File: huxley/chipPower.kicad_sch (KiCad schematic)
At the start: 5 parts, among them J1 Conn_01x01_Socket, J2 Conn_01x01_Socket, J3 Conn_01x01_Socket, J4 Conn_Coaxial_Power

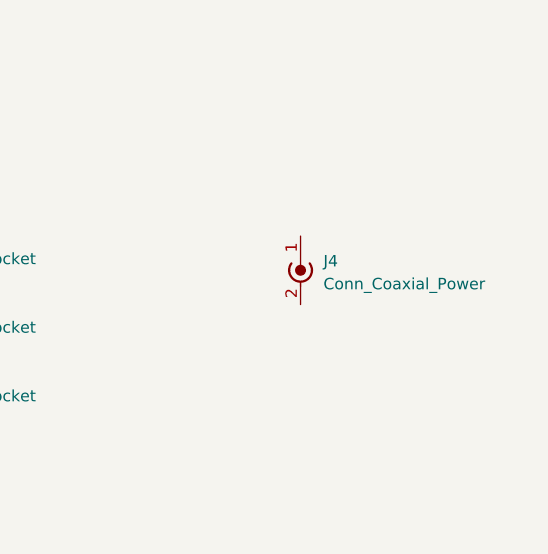
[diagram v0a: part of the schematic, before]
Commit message: added analog chip schematics and connector footprints
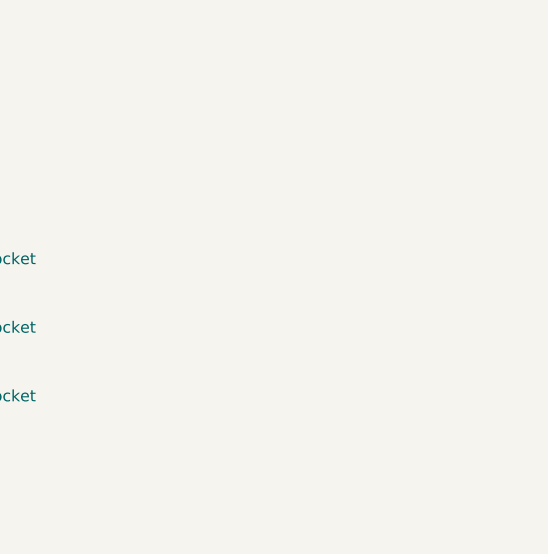
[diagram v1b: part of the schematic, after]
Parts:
- removed J4: Conn_Coaxial_Power, symbol Connector:Conn_Coaxial_Power
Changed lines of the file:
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@@
-	)
-	(symbol
-		(lib_id "Connector:Conn_Coaxial_Power")
-		(at 190.5 55.88 0)
-		(unit 1)
-		(exclude_from_sim no)
-		(in_bom yes)
-		(on_board yes)
-		(dnp no)
-		(fields_autoplaced yes)
-		(property "Reference" "J4"
-			(at 193.04 56.1339 0)
-			(effects
-				(font
-					(size 1.27 1.27)
-				)
-				(justify left)
-			)
-		)
-		(property "Value" "Conn_Coaxial_Power"
-			(at 193.04 58.6739 0)
-			(effects
-				(font
-					(size 1.27 1.27)
-				)
-				(justify left)
-			)
-		)
-		(property "Footprint" ""
-			(at 190.5 57.15 0)
-			(effects
-				(font
-					(size 1.27 1.27)
-				)
-				(hide yes)
-			)
-		)
-		(property "Datasheet" "~"
-			(at 190.5 57.15 0)
-			(effects
-				(font
-					(size 1.27 1.27)
-				)
-				(hide yes)
-			)
-		)
-		(property "Description" "coaxial connector (BNC, SMA, SMB, SMC, Cinch/RCA, LEMO, ...)"
-			(at 190.5 55.88 0)
-			(effects
-				(font
-					(size 1.27 1.27)
-				)
-				(hide yes)
-			)
-		)
-		(pin "1"
-		)
-		(pin "2"
-		)
-		(instances
-			(project "huxley"
-				(path "/c6103430-c27a-4e90-8e2e-9404255f5ee3/ab3d06fa-a7a0-4394-b6d7-1ca538756c6f"
-					(reference "J4")
-					(unit 1)
-				)
-			)
-		)
 	)
 	(symbol

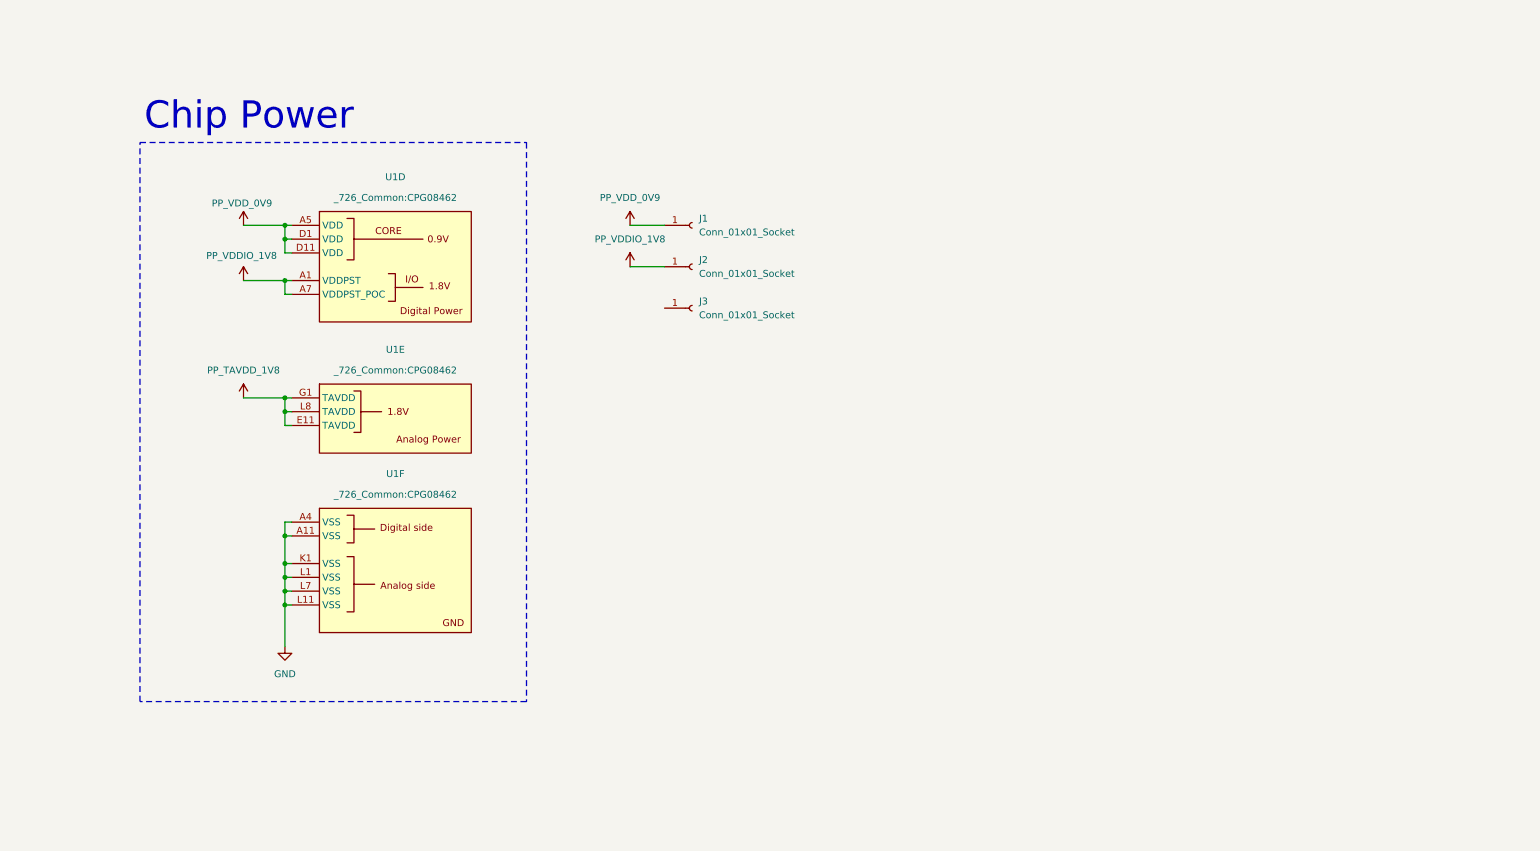
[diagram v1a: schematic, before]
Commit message: updated Ibias gen and footprints
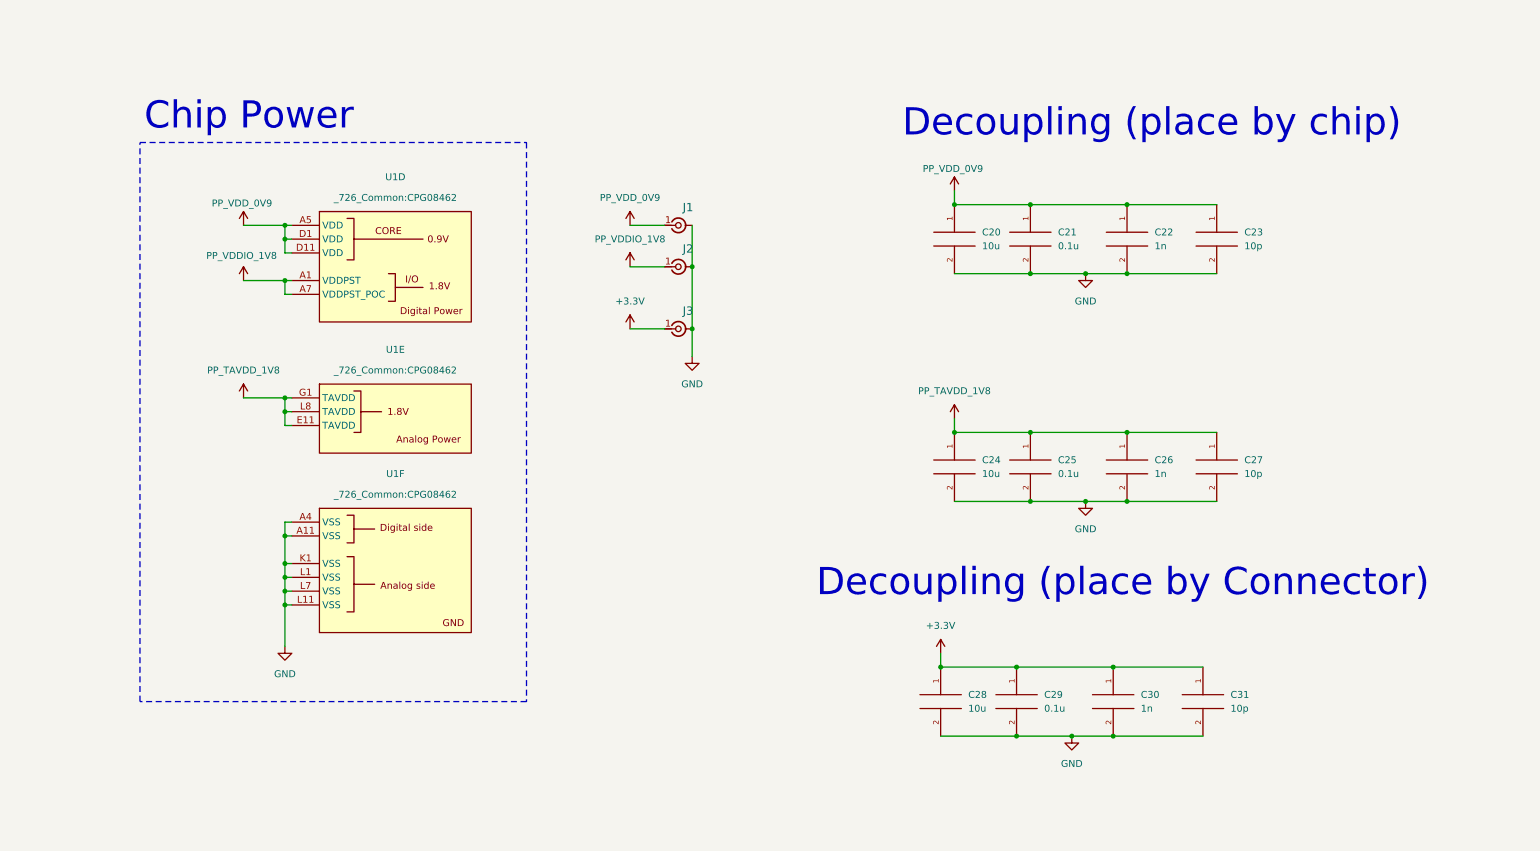
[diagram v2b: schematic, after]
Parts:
- removed J1, J2, J3: Conn_01x01_Socket, symbol Connector:Conn_01x01_Socket
- added C20, C24, C28: 10u, Capacitor_SMD:C_0402_1005Metric, symbol pspice:C
- added C21, C25, C29: 0.1u, Capacitor_SMD:C_0402_1005Metric, symbol pspice:C
- added C22, C26, C30: 1n, Capacitor_SMD:C_0402_1005Metric, symbol pspice:C
- added C23, C27, C31: 10p, Capacitor_SMD:C_0402_1005Metric, symbol pspice:C
- added J1, J2, J3: SMA_RF2-04A-T-00-50-G, 726_footprints:CONN_RF2-04A-T-00-50-G_ADM, symbol _PHASE:SMA_RF2-04A-T-00-50-G
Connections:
- net GND: now also C20.2, C21.2, C22.2, C23.2, C24.2, C25.2, C26.2, C27.2, C28.2, C29.2, C30.2, C31.2, J1., J1.3 (Ext), J1.4 (Ext), J1.5 (Ext), J2., J2.3 (Ext), J2.4 (Ext), J2.5 (Ext), J3., J3.3 (Ext), J3.4 (Ext), J3.5 (Ext)
- net PP_TAVDD_1V8: now also C24.1, C25.1, C26.1, C27.1
- net PP_VDDIO_1V8: now also J2.1
- net PP_VDD_0V9: now also C20.1, C21.1, C22.1, C23.1, J1.1
- new net +3.3V: C28.1, C29.1, C30.1, C31.1, J3.1
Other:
- note added: "Decoupling (place by Connector)"
- note added: "Decoupling (place by chip)"

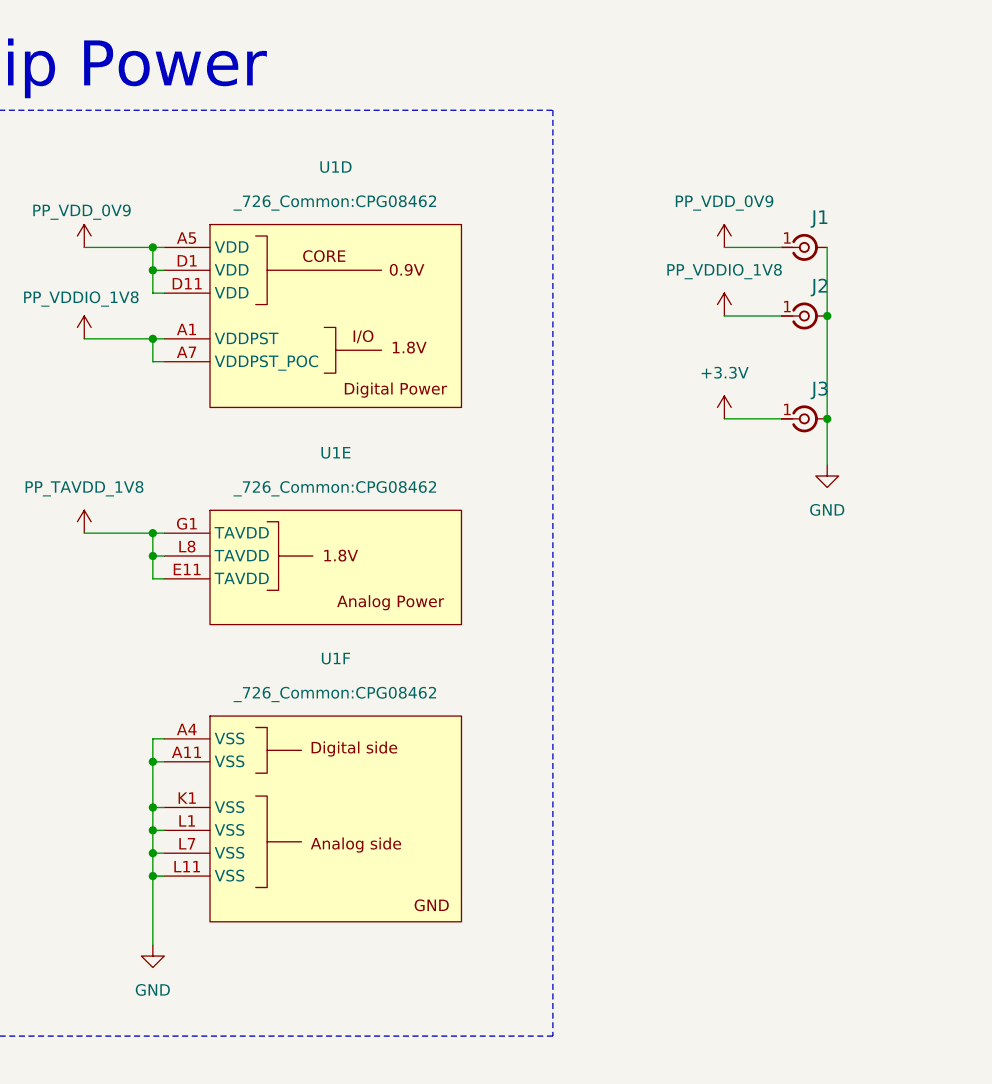
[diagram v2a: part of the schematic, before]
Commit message: updated footprints
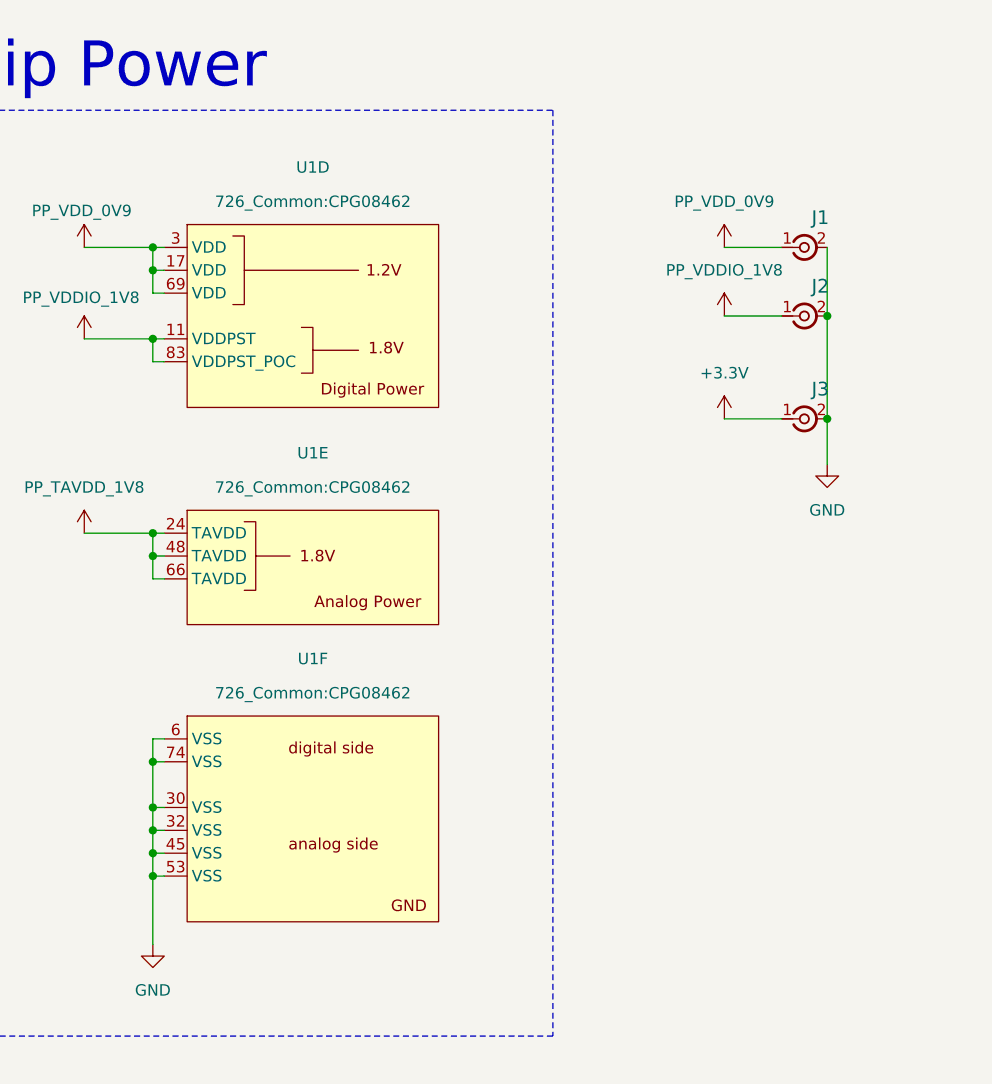
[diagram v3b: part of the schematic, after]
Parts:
- U1: footprint _726_Common:CPG08462 -> 726_Common:CPG08462
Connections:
- net GND: now also J1.2, J2.2, J3.2, U1.30 (VSS), U1.32 (VSS), U1.45 (VSS), U1.53 (VSS), U1.6 (VSS), U1.74 (VSS); no longer J1., J2., J3., U1.A11 (VSS), U1.A4 (VSS), U1.K1 (VSS), U1.L1 (VSS), U1.L11 (VSS), U1.L7 (VSS)
- net PP_TAVDD_1V8: now also U1.24 (TAVDD), U1.48 (TAVDD), U1.66 (TAVDD); no longer U1.E11 (TAVDD), U1.G1 (TAVDD), U1.L8 (TAVDD)
- net PP_VDDIO_1V8: now also U1.11 (VDDPST), U1.83 (VDDPST_POC); no longer U1.A1 (VDDPST), U1.A7 (VDDPST_POC)
- net PP_VDD_0V9: now also U1.17 (VDD), U1.3 (VDD), U1.69 (VDD); no longer U1.A5 (VDD), U1.D1 (VDD), U1.D11 (VDD)
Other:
- moved on the sheet: U1E

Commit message: layout
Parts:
- added C32: 10u, Capacitor_SMD:C_0402_1005Metric, symbol pspice:C
- added C33: 0.1u, Capacitor_SMD:C_0402_1005Metric, symbol pspice:C
- added C34: 1n, Capacitor_SMD:C_0402_1005Metric, symbol pspice:C
- added C35: 10p, Capacitor_SMD:C_0402_1005Metric, symbol pspice:C
- added J5: SMA_RF2-04A-T-00-50-G, 726_footprints:CONN_RF2-04A-T-00-50-G_ADM, symbol _PHASE:SMA_RF2-04A-T-00-50-G
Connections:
- net GND: now also C32.2, C33.2, C34.2, C35.2, J5.2, J5.3 (Ext), J5.4 (Ext), J5.5 (Ext)
- net PP_TAVDD_1V8: now also J5.1
- net PP_VDDIO_1V8: now also C32.1, C33.1, C34.1, C35.1
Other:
- moved on the sheet: C20, C21, C22, C23

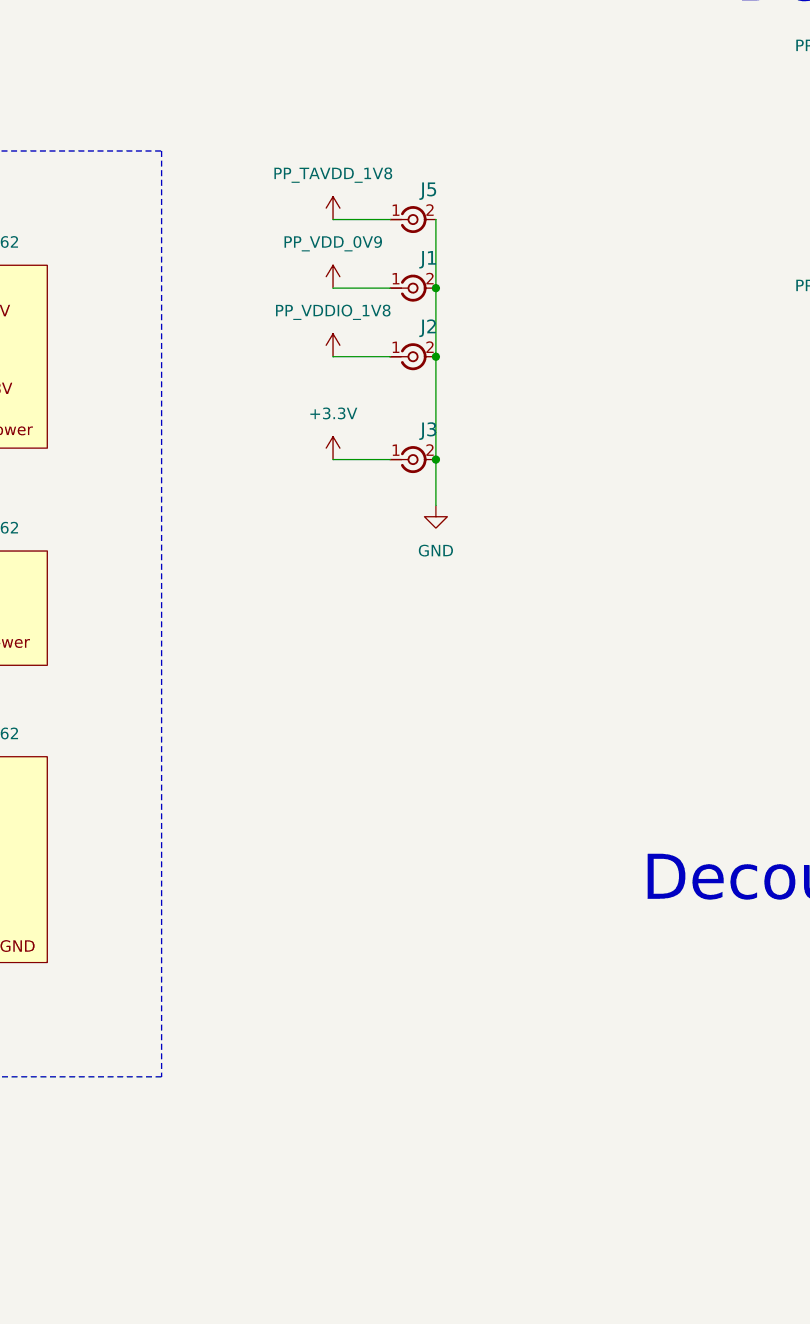
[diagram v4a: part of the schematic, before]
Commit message: added banana plugs and fixed analog discovery pinout
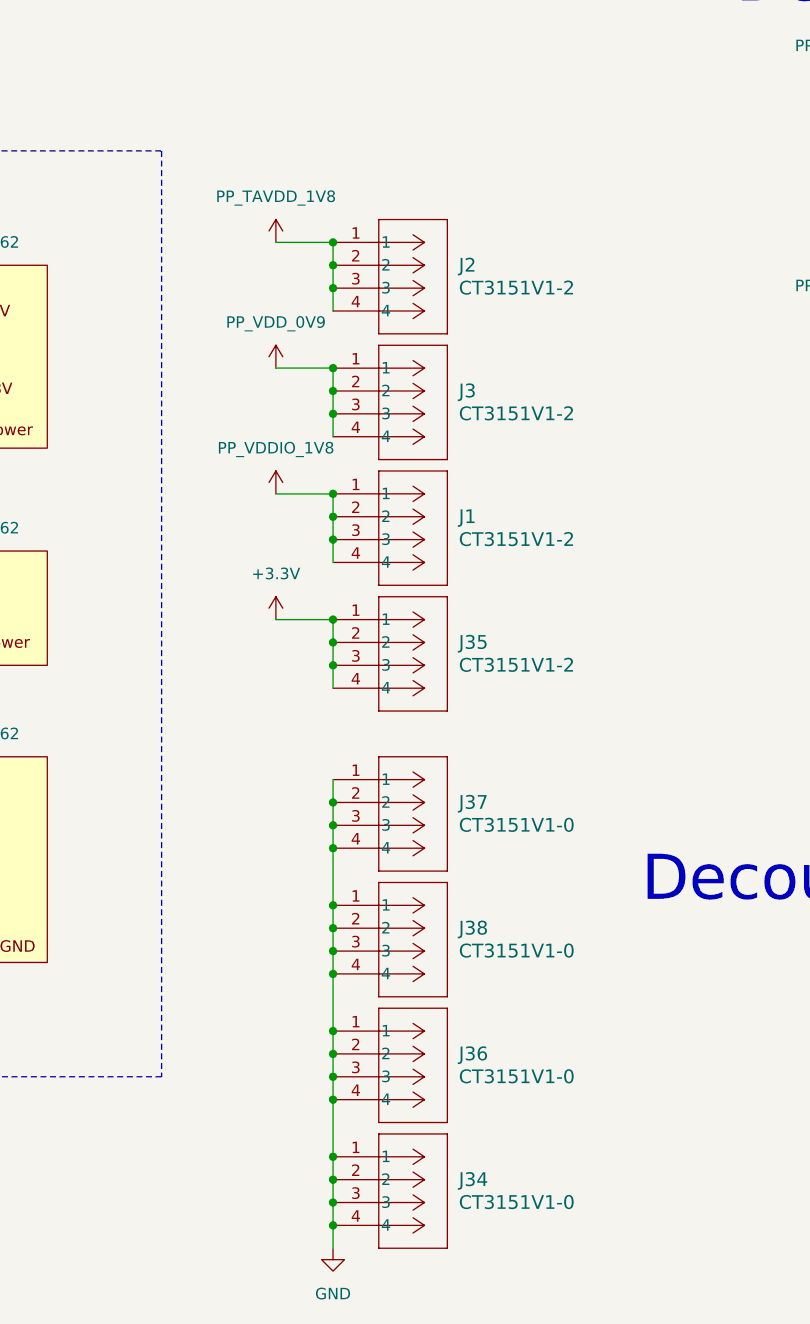
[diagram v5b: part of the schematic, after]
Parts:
- removed J1, J2, J3, J5: SMA_RF2-04A-T-00-50-G, 726_footprints:CONN_RF2-04A-T-00-50-G_ADM, symbol _PHASE:SMA_RF2-04A-T-00-50-G
- added J1, J2, J3, J35: CT3151V1-2, 726_footprints:banana_plug_CT3151V1-0, symbol _PHASE:CT3151V1-0
- added J34, J36, J37, J38: CT3151V1-0, 726_footprints:banana_plug_CT3151V1-0, symbol _PHASE:CT3151V1-0
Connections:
- net +3.3V: now also J35.1, J35.2, J35.3, J35.4
- net GND: now also J34.1, J34.2, J34.3, J34.4, J36.1, J36.2, J36.3, J36.4, J37.1, J37.2, J37.3, J37.4, J38.1, J38.2, J38.3, J38.4
- net PP_TAVDD_1V8: now also J2.1, J2.2, J2.3, J2.4
- net PP_VDDIO_1V8: now also J1.1, J1.2, J1.3, J1.4
- net PP_VDD_0V9: now also J3.1, J3.2, J3.3, J3.4

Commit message: layout_1003
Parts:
- removed J36, J38: CT3151V1-0, 726_footprints:banana_plug_CT3151V1-0, symbol _PHASE:CT3151V1-0
- C20, C21, C22, C23, C24, C25, C26, C27, C28, C29, C30, C31, C32, C33, C34, C35: footprint Capacitor_SMD:C_0402_1005Metric -> Capacitor_SMD:C_0603_1608Metric
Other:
- moved on the sheet: J34

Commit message: layout_1003_2
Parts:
- U1: footprint 726_Common:CPG08462 -> 0_726_footprints:CPG08462_Full; symbol _PHASE:PHASEIC_SOCKET -> 0_PHASE:PHASEIC_SOCKET
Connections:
- net GND: no longer U1.30 (VSS), U1.32 (VSS), U1.45 (VSS), U1.53 (VSS), U1.6 (VSS), U1.74 (VSS)
- net PP_TAVDD_1V8: no longer U1.24 (TAVDD), U1.48 (TAVDD), U1.66 (TAVDD)
- net PP_VDDIO_1V8: no longer U1.11 (VDDPST), U1.83 (VDDPST_POC)
- net PP_VDD_0V9: no longer U1.17 (VDD), U1.3 (VDD), U1.69 (VDD)
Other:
- moved on the sheet: U1E
